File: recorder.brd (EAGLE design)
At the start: 22.4 x 41 mm, 46 parts, among them M1 ELECTRET_MICROPHON-WM-61A, Q1 4.096MHz, T1 MMBT3904 NPN, U1 ISD15100

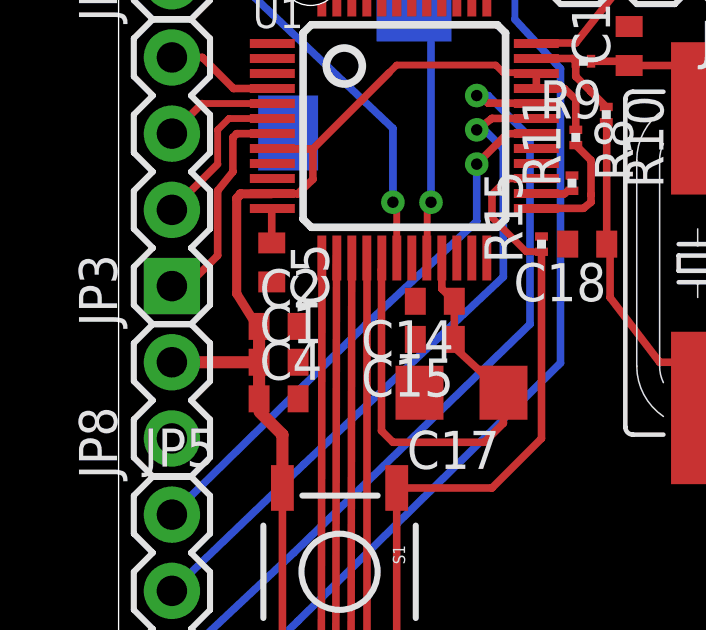
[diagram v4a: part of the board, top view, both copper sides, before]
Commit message: added design parameters readMe, BoM, changed C1 package to 1206
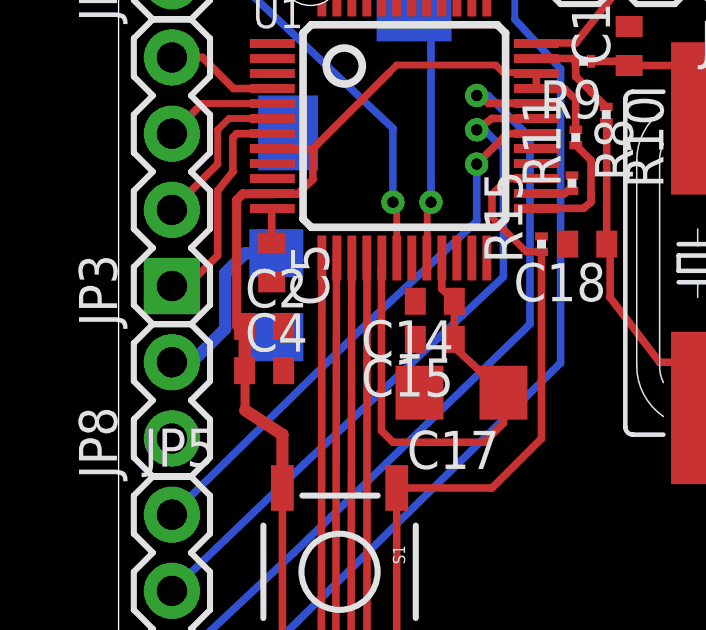
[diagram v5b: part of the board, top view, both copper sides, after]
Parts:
- C1: device rcl:C0402 -> rcl:C1206
- moved C1 2.24 mm to (28.1, 56.6), flipped to the bottom, turned to 270 degrees
- moved C4 1.06 mm to (27.7, 54.1)
- moved C2 0.48 mm to (27.7, 55.5)
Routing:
- net VCCD: track 35.6 -> 39.1 mm
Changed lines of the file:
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@@
 <grid distance="0.05" unitdist="inch" unit="inch" style="lines" multiple="1" display="no" altdistance="0.001" altunitdist="inch" altunit="inch"/>
 <layers>
-<layer number="1" name="Top" color="4" fill="1" visible="no" active="yes"/>
-<layer number="16" name="Bottom" color="1" fill="1" visible="yes" active="yes"/>
+<layer number="1" name="Top" color="4" fill="1" visible="yes" active="yes"/>
+<layer number="16" name="Bottom" color="1" fill="1" visible="no" active="yes"/>
 <layer number="17" name="Pads" color="2" fill="1" visible="yes" active="yes"/>
 <layer number="18" name="Vias" color="2" fill="1" visible="yes" active="yes"/>
 <layer number="19" name="Unrouted" color="6" fill="1" visible="yes" active="yes"/>
 <layer number="20" name="Dimension" color="15" fill="1" visible="yes" active="yes"/>
-<layer number="21" name="tPlace" color="41" fill="1" visible="no" active="yes"/>
-<layer number="22" name="bPlace" color="14" fill="1" visible="yes" active="yes"/>
-<layer number="23" name="tOrigins" color="15" fill="1" visible="no" active="yes"/>
-<layer number="24" name="bOrigins" color="15" fill="1" visible="yes" active="yes"/>
+<layer number="21" name="tPlace" color="41" fill="1" visible="yes" active="yes"/>
+<layer number="22" name="bPlace" color="14" fill="1" visible="no" active="yes"/>
+<layer number="23" name="tOrigins" color="15" fill="1" visible="yes" active="yes"/>
+<layer number="24" name="bOrigins" color="15" fill="1" visible="no" active="yes"/>
 <layer number="25" name="tNames" color="7" fill="1" visible="no" active="yes"/>
 <layer number="26" name="bNames" color="7" fill="1" visible="no" active="yes"/>
@@
 <layer number="49" name="Reference" color="7" fill="1" visible="no" active="yes"/>
 <layer number="50" name="dxf" color="7" fill="1" visible="no" active="no"/>
-<layer number="51" name="tDocu" color="6" fill="1" visible="no" active="yes"/>
-<layer number="52" name="bDocu" color="17" fill="1" visible="yes" active="yes"/>
+<layer number="51" name="tDocu" color="6" fill="1" visible="yes" active="yes"/>
+<layer number="52" name="bDocu" color="17" fill="1" visible="no" active="yes"/>
 <layer number="53" name="tGND_GNDA" color="7" fill="9" visible="no" active="no"/>
 <layer number="54" name="bGND_GNDA" color="1" fill="9" visible="no" active="no"/>
@@
 <element name="C18" library="rcl" package="C0402" value="27pF" x="38.481" y="58.293" rot="R180"/>
 <element name="C8" library="rcl" package="C0402" value="0.1uF" x="33.655" y="70.485" rot="MR180"/>
-<element name="C1" library="rcl" package="C0402" value="47uF" x="28.194" y="54.356"/>
-<element name="C2" library="rcl" package="C0402" value="0.01uF" x="28.194" y="55.5498"/>
-<element name="C4" library="rcl" package="C0402" value="0.001uF" x="28.194" y="53.1368"/>
+<element name="C2" library="rcl" package="C0402" value="0.01uF" x="27.7114" y="55.5498"/>
+<element name="C4" library="rcl" package="C0402" value="0.001uF" x="27.7114" y="54.0766"/>
 <element name="C13" library="rcl" package="C0402" value="0.1uF" x="34.544" y="71.374" rot="R90"/>
 <element name="C11" library="rcl" package="C0402" value="0.1uF" x="31.4198" y="70.3834" rot="R180"/>
@@
 <element name="JP3" library="SparkFun-Connectors" package="1X04" value="" x="24.638" y="56.896" rot="R90"/>
 <element name="JP8" library="SparkFun-Connectors" package="1X02" value="M02PTH" x="24.638" y="51.816" rot="R90"/>
+<element name="C1" library="rcl" package="C1206" value="47uF" x="28.1178" y="56.5912" rot="MR270"/>
 </elements>
 <signals>
@@
 <wire x1="37.719" y1="63.4746" x2="38.1" y2="63.119" width="0.254" layer="1"/>
 <wire x1="38.1" y1="63.119" x2="38.1" y2="62.104" width="0.254" layer="1"/>
-<wire x1="27.508" y1="53.431" x2="27.544" y2="53.1368" width="0.254" layer="1"/>
 <wire x1="36.765" y1="63.5" x2="36.785" y2="63.48" width="0.254" layer="1"/>
 <wire x1="28.321" y1="50.165" x2="28.321" y2="44.577" width="0.254" layer="1"/>
@@
 <wire x1="29.337" y1="61.468" x2="29.337" y2="60.452" width="0.254" layer="1"/>
 <wire x1="29.337" y1="60.452" x2="28.829" y2="59.9694" width="0.254" layer="1"/>
-<wire x1="26.797" y1="59.817" x2="26.797" y2="56.642" width="0.3048" layer="1"/>
-<wire x1="26.797" y1="56.642" x2="27.410596875" y2="55.660246875" width="0.3048" layer="1"/>
-<wire x1="27.410596875" y1="55.660246875" x2="27.432" y2="55.626" width="0.254" layer="1"/>
-<wire x1="26.797" y1="59.817" x2="26.924" y2="59.9694" width="0.3048" layer="1"/>
-<wire x1="26.924" y1="59.9694" x2="27.949" y2="59.9694" width="0.3048" layer="1"/>
-<wire x1="27.949" y1="59.9694" x2="27.985" y2="59.98" width="0.254" layer="1"/>
+<wire x1="26.927996875" y1="55.660246875" x2="26.9494" y2="55.626" width="0.254" layer="1"/>
 <wire x1="28.829" y1="59.9694" x2="28.021" y2="59.9694" width="0.254" layer="1"/>
 <wire x1="28.021" y1="59.9694" x2="27.985" y2="59.98" width="0.254" layer="1"/>
 <wire x1="28.321" y1="50.165" x2="28.321" y2="51.943" width="0.4064" layer="1"/>
-<wire x1="28.321" y1="51.943" x2="27.559" y2="52.705" width="0.4064" layer="1"/>
-<wire x1="27.559" y1="53.452" x2="27.544" y2="53.1368" width="0.254" layer="1"/>
+<wire x1="28.321" y1="51.943" x2="27.0764" y2="52.7558" width="0.4064" layer="1"/>
+<wire x1="27.0764" y1="53.452" x2="27.0614" y2="54.0766" width="0" layer="19" extent="1-16"/>
 <wire x1="36.765" y1="63.5" x2="36.576" y2="63.5" width="0.254" layer="1"/>
 <wire x1="31.877" y1="64.008" x2="32.131" y2="64.262" width="0.2286" layer="1"/>
@@
 <wire x1="35.433" y1="64.262" x2="35.687" y2="64.008" width="0.2286" layer="1"/>
 <wire x1="35.687" y1="64.008" x2="36.195" y2="64.008" width="0.2286" layer="1"/>
+<contactref element="JP8" pad="2"/>
+<wire x1="27.0614" y1="55.5498" x2="27.02075" y2="55.753" width="0.254" layer="1"/>
+<wire x1="27.02075" y1="55.753" x2="26.927996875" y2="55.660246875" width="0.254" layer="1"/>
 <contactref element="C1" pad="1"/>
-<contactref element="JP8" pad="2"/>
-<wire x1="27.544" y1="55.5498" x2="27.50335" y2="55.753" width="0.254" layer="1"/>
-<wire x1="27.50335" y1="55.753" x2="27.410596875" y2="55.660246875" width="0.254" layer="1"/>
-<wire x1="27.544" y1="53.1368" x2="27.544" y2="54.356" width="0.4064" layer="1"/>
-<wire x1="27.544" y1="54.356" x2="27.544" y2="55.5498" width="0.4064" layer="1"/>
-<wire x1="27.544" y1="54.356" x2="24.638" y2="54.356" width="0.4064" layer="1"/>
+<wire x1="28.1178" y1="57.9912" x2="27.0794" y2="57.9912" width="0.4064" layer="16"/>
+<wire x1="27.0794" y1="57.9912" x2="26.416" y2="57.3278" width="0.4064" layer="16"/>
+<wire x1="26.416" y1="57.3278" x2="26.416" y2="55.4736" width="0.4064" layer="16"/>
+<wire x1="26.416" y1="55.4736" x2="25.273" y2="54.3306" width="0.4064" layer="16"/>
+<wire x1="25.273" y1="54.3306" x2="24.6634" y2="54.3306" width="0.4064" layer="16"/>
+<wire x1="24.6634" y1="54.3306" x2="24.638" y2="54.356" width="0.4064" layer="16"/>
+<wire x1="27.0614" y1="55.5498" x2="27.0614" y2="54.0766" width="0.4064" layer="1"/>
+<wire x1="28.021" y1="59.9694" x2="27.0002" y2="59.9694" width="0.3048" layer="1"/>
+<wire x1="27.0002" y1="59.9694" x2="26.797" y2="59.7662" width="0.3048" layer="1"/>
+<wire x1="26.797" y1="59.7662" x2="26.797" y2="55.5602" width="0.3048" layer="1"/>
+<wire x1="26.797" y1="55.5602" x2="27.0614" y2="55.5498" width="0.3048" layer="1"/>
 <wire x1="36.195" y1="64.008" x2="36.785" y2="63.98" width="0" layer="19" extent="1-1"/>
-<wire x1="27.559" y1="52.705" x2="27.544" y2="53.1368" width="0" layer="19" extent="1-1"/>
+<wire x1="26.416" y1="55.4736" x2="26.927996875" y2="55.660246875" width="0" layer="19" extent="1-16"/>
+<wire x1="27.0764" y1="52.7558" x2="27.0764" y2="54.0616" width="0.3048" layer="1"/>
+<wire x1="27.0764" y1="54.0616" x2="27.0614" y2="54.0766" width="0.3048" layer="1"/>
+<wire x1="27.0254" y1="53.431" x2="27.0614" y2="54.0766" width="0" layer="19" extent="1-16"/>
 </signal>
 <signal name="N$17">
@@
 <contactref element="R5" pad="1"/>
 <contactref element="C2" pad="2"/>
-<contactref element="C1" pad="2"/>
 <contactref element="C4" pad="2"/>
 <contactref element="U1" pad="9"/>
@@
 <contactref element="U1" pad="19"/>
 <contactref element="JP8" pad="1"/>
+<contactref element="C1" pad="2"/>
 <wire x1="39.032" y1="71.816" x2="40.641" y2="73.152" width="0" layer="19" extent="16-16"/>
 <wire x1="37.338" y1="71.135" x2="39.032" y2="71.816" width="0" layer="19" extent="16-16"/>
@@
 <wire x1="32.751" y1="55.118" x2="32.751" y2="56.388" width="0" layer="19" extent="1-1"/>
 <wire x1="32.89" y1="53.34" x2="32.751" y2="55.118" width="0" layer="19" extent="1-1"/>
-<wire x1="28.844" y1="55.5498" x2="32.751" y2="55.118" width="0" layer="19" extent="1-1"/>
-<wire x1="28.844" y1="54.356" x2="28.844" y2="55.5498" width="0" layer="19" extent="1-1"/>
-<wire x1="28.844" y1="53.1368" x2="28.844" y2="54.356" width="0" layer="19" extent="1-1"/>
-<wire x1="27.9654" y1="57.0334" x2="28.844" y2="55.5498" width="0" layer="19" extent="1-1"/>
+<wire x1="28.3614" y1="55.5498" x2="32.751" y2="55.118" width="0" layer="19" extent="1-1"/>
+<wire x1="28.1178" y1="55.1912" x2="28.3614" y2="55.5498" width="0" layer="19" extent="1-16"/>
+<wire x1="27.9654" y1="57.0334" x2="28.3614" y2="55.5498" width="0" layer="19" extent="1-1"/>
+<wire x1="28.3614" y1="54.0766" x2="28.1178" y2="55.1912" width="0" layer="19" extent="1-16"/>
 <wire x1="27.985" y1="60.48" x2="27.9654" y2="57.0334" width="0" layer="19" extent="1-1"/>
 <wire x1="27.985" y1="60.98" x2="27.985" y2="60.48" width="0" layer="19" extent="1-1"/>
-<wire x1="24.638" y1="51.816" x2="28.844" y2="53.1368" width="0" layer="19" extent="1-1"/>
+<wire x1="24.638" y1="51.816" x2="28.3614" y2="54.0766" width="0" layer="19" extent="1-1"/>
 <wire x1="24.638" y1="67.056" x2="27.985" y2="60.98" width="0" layer="19" extent="1-1"/>
 <wire x1="27.3454" y1="72.1614" x2="24.638" y2="67.056" width="0" layer="19" extent="1-1"/>
